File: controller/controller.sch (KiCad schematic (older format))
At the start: 30 parts, among them J1 Arduino_Nano_Header, P1 CONN_01X03, P2 CONN_01X03, P3 CONN_01X07, P4 CONN_01X02, SW1 DIPS_10, U1 MAX5024, U3 IL610, U4 MAX3040, U5 74LS165, U6 74LS165

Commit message: REV1 boards ordered
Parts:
- added P5: CONN_01X11, Pin_Headers:Pin_Header_Straight_1x11, symbol CONN_01X11
- added P6: CONN_01X08, Pin_Headers:Pin_Header_Straight_1x08, symbol CONN_01X08
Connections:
- net +5V: now also J1.30 (VIN); no longer J1.27 (5V)
- net DATA: now also P5.10 (P10)
- net DXM_OK: now also P5.8 (P8)
- net LATCH: now also P5.9 (P9)
- net at J1.8 (D5/T1), U4.1 (T1IN): now also P5.4 (P4)
- net at J1.7 (D4/T0), U4.7 (T2IN): now also P5.3 (P3)
- net at J1.10 (D7/AIN1): now also P5.6 (P6)
- net at J1.11 (D8/ICP): now also P5.7 (P7)
- net at J1.15 (D12/MISO): now also P5.11 (P11)
- net at J1.19 (A0): now also P6.8 (P8)
- net at J1.20 (A1): now also P6.7 (P7)
- net at J1.21 (A2): now also P6.6 (P6)
- net at J1.22 (A3): now also P6.5 (P5)
- net at J1.23 (A4): now also P6.4 (P4)
- net at J1.24 (A5): now also P6.3 (P3)
- net at J1.25 (A6): now also P6.2 (P2)
- net at C7.1, J1.26 (A7), RV1.2: now also P6.1 (P1)
- net RESET: now reaches J1.28 (RESET)
- net RESET: now also U1.4 (~RESET)
- net at J1.5 (D2/INT0): now also P5.1 (P1)
- net at J1.6 (D3/INT1): now also P5.2 (P2)
- net at J1.9 (D6/AIN0): now also P5.5 (P5)

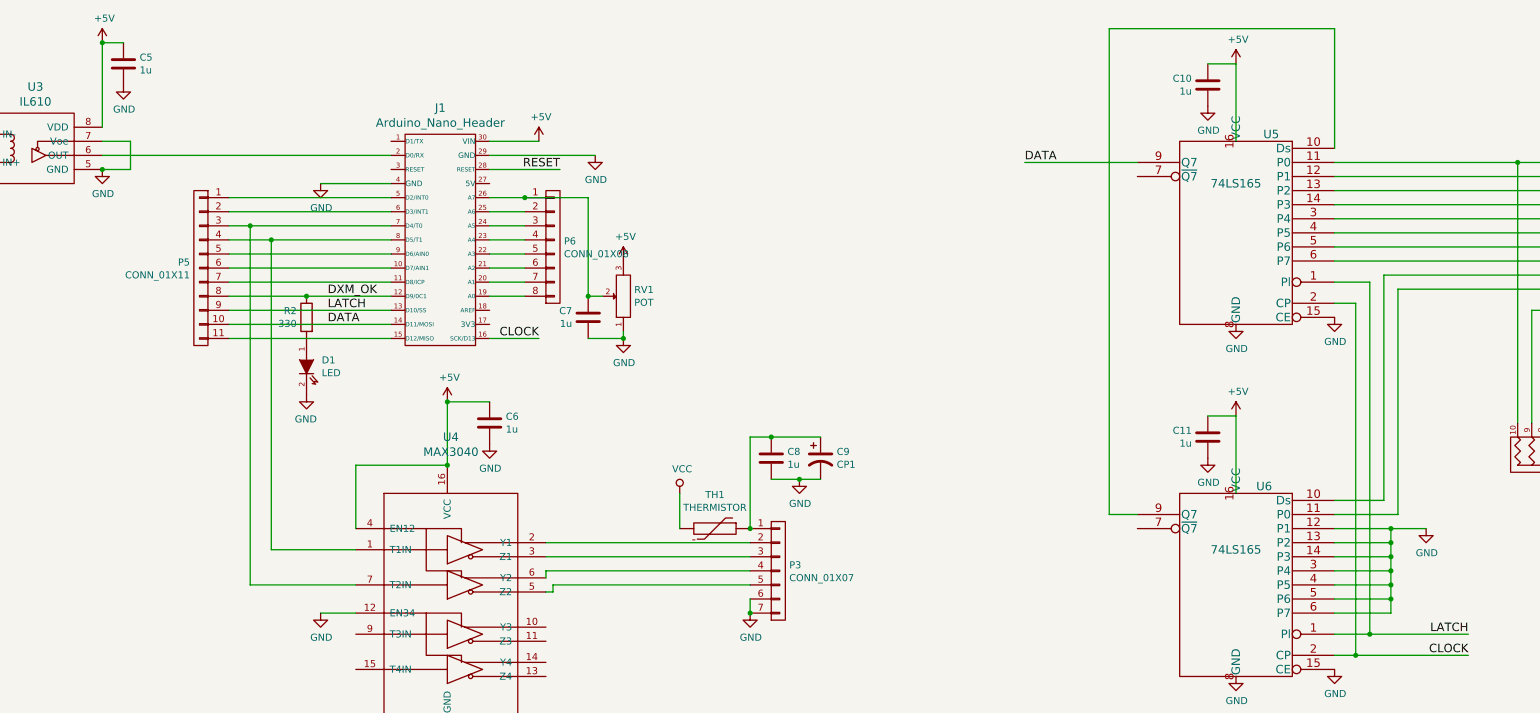
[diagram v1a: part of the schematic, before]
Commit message: Add fixes: control receiver enable line from Arduino so it does not interfere with programming; move data line to MISO pin so that we can read dip switch via SPI; fix routing for U6;
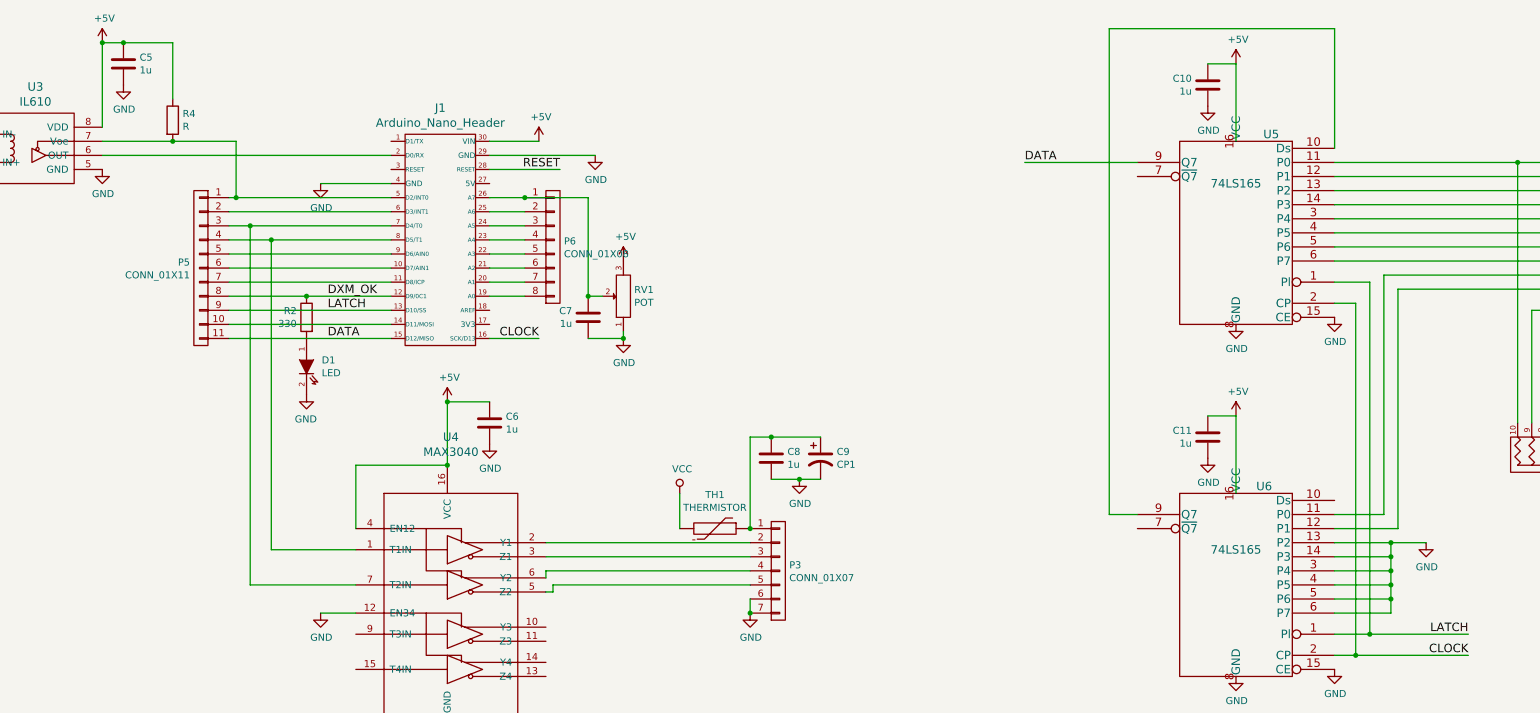
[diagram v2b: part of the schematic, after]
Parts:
- added R4: R, Resistors_SMD:R_0603_HandSoldering, symbol R
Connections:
- net +5V: now also R4.1
- net DATA: now also J1.15 (D12/MISO), P5.11 (P11); no longer J1.14 (D11/MOSI), P5.10 (P10)
- net GND: no longer U3.7 (Voe), U6.12 (P1)
- net at J1.5 (D2/INT0), P5.1 (P1): now also U3.7 (Voe), R4.2
- net at R1.1, SW1.11: now also U6.12 (P1); no longer U6.11 (P0)
- net at RP1.2 (P2), SW1.12: now also U6.11 (P0); no longer U6.10 (Ds)
- new net: J1.14 (D11/MOSI), P5.10 (P10)
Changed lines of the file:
@@
 LIBS:contrib
 LIBS:valves
-LIBS:max3096
 LIBS:w_connectors
 LIBS:dips-s
+LIBS:max3096
 LIBS:controller-cache
 EELAYER 25 0
@@
 L GND #PWR32
 U 1 1 571643DD
-P 12500 4450
-F 0 "#PWR32" H 12500 4200 50  0001 C CNN
-F 1 "GND" H 12505 4277 50  0000 C CNN
-F 2 "" H 12500 4450 60  0000 C CNN
-F 3 "" H 12500 4450 60  0000 C CNN
-	1    12500 4450
+P 12500 4550
+F 0 "#PWR32" H 12500 4300 50  0001 C CNN
+F 1 "GND" H 12505 4377 50  0000 C CNN
+F 2 "" H 12500 4550 60  0000 C CNN
+F 3 "" H 12500 4550 60  0000 C CNN
+	1    12500 4550
 	1    0    0    -1
 $EndComp
@@
 	1    0    0    -1
 $EndComp
-Text Label 4700 3000 0    60   ~ 0
+Text Label 4700 3100 0    60   ~ 0
 DATA
 Text Label 6200 3100 2    60   ~ 0
@@
 Connection ~ 7100 8150
 Wire Wire Line
-	3250 1000 3100 1000
+	3100 1000 3600 1000
 Wire Wire Line
 	3100 1000 3100 1600
 Connection ~ 3100 1000
-Wire Wire Line
-	3100 1700 3300 1700
-Wire Wire Line
-	3300 1700 3300 1900
-Wire Wire Line
-	3300 1900 3100 1900
-Connection ~ 3100 1900
 Wire Wire Line
 	5150 1800 3100 1800
@@
 	11850 5200 12800 5200
 Wire Wire Line
-	12200 2650 12200 4250
-Wire Wire Line
-	12200 4250 11850 4250
-Wire Wire Line
-	12300 2750 12300 4350
-Wire Wire Line
-	12300 4350 11850 4350
-Wire Wire Line
-	11850 4450 12500 4450
+	12300 2750 12300 4450
 Wire Wire Line
 	12250 5050 11850 5050
 Wire Wire Line
-	12250 4450 12250 5050
-Connection ~ 12250 4450
-Wire Wire Line
-	11850 4950 12250 4950
+	12250 4950 11850 4950
 Connection ~ 12250 4950
 Wire Wire Line
-	11850 4850 12250 4850
+	12250 4850 11850 4850
 Connection ~ 12250 4850
 Wire Wire Line
-	11850 4750 12250 4750
+	12250 4750 11850 4750
 Connection ~ 12250 4750
 Wire Wire Line
@@
 Connection ~ 12250 4650
 Wire Wire Line
-	11850 4550 12250 4550
+	11850 4550 12500 4550
 Connection ~ 12250 4550
 Connection ~ 12100 5200
@@
 $EndComp
 Wire Wire Line
-	5150 2100 4000 2100
+	4000 2100 5150 2100
 Wire Wire Line
 	5150 2200 4000 2200
@@
 Wire Wire Line
 	6100 2800 5850 2800
+$Comp
+L R R4
+U 1 1 571FBE18
+P 3600 1550
+F 0 "R4" H 3670 1596 50  0000 L CNN
+F 1 "R" H 3670 1505 50  0000 L CNN
+F 2 "Resistors_SMD:R_0603_HandSoldering" V 3530 1550 30  0001 C CNN
+F 3 "" H 3600 1550 30  0000 C CNN
+	1    3600 1550
+	1    0    0    -1
+$EndComp
+Wire Wire Line
+	3100 1700 4050 1700
+Wire Wire Line
+	3600 1000 3600 1400
+Connection ~ 3250 1000
+Wire Wire Line
+	4050 1700 4050 2100
+Connection ~ 4050 2100
+Connection ~ 3600 1700
 Connection ~ 6100 2100
+Wire Wire Line
+	12250 4550 12250 5050
+Wire Wire Line
+	12300 4450 11850 4450
+Wire Wire Line
+	12200 2650 12200 4350
+Wire Wire Line
+	12200 4350 11850 4350
 $EndSCHEMATC

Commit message: Add fixes to PCB
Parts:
- removed P5: CONN_01X11, Pin_Headers:Pin_Header_Straight_1x11, symbol CONN_01X11
- added P5: CONN_01X10, symbol CONN_01X10
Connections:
- net DATA: now also P5.10 (P10)
- net DXM_OK: now also P5.7 (P7)
- net LATCH: now also P5.8 (P8)
- net at J1.8 (D5/T1), U4.1 (T1IN): now also P5.3 (P3)
- net at J1.7 (D4/T0), U4.7 (T2IN): now also P5.2 (P2)
- net at J1.10 (D7/AIN1): now also P5.5 (P5)
- net at J1.11 (D8/ICP): now also P5.6 (P6)
- net at J1.14 (D11/MOSI): now also P5.9 (P9)
- net at J1.6 (D3/INT1): now also P5.1 (P1)
- net at J1.9 (D6/AIN0): now also P5.4 (P4)
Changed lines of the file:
@@
 taupyti elektrą:\n* tiny441 vietoj arduino?
 Wire Wire Line
-	6300 8150 7100 8150
-Wire Wire Line
-	4150 8450 4650 8450
+	6300 8150 6450 8150
+Wire Wire Line
+	6450 8150 6800 8150
+Wire Wire Line
+	6800 8150 7100 8150
+Wire Wire Line
+	4150 8450 4500 8450
+Wire Wire Line
+	4500 8450 4650 8450
 Connection ~ 7100 8450
 Connection ~ 4500 8450
 Wire Wire Line
-	3400 8150 5000 8150
+	3400 8150 4150 8150
+Wire Wire Line
+	4150 8150 4500 8150
+Wire Wire Line
+	4500 8150 4850 8150
+Wire Wire Line
+	4850 8150 5000 8150
 Connection ~ 4150 8150
 Connection ~ 7100 8150
 Wire Wire Line
-	3100 1000 3600 1000
+	3100 1000 3250 1000
+Wire Wire Line
+	3250 1000 3600 1000
 Wire Wire Line
 	3100 1000 3100 1600
@@
 Connection ~ 5550 3550
 Wire Wire Line
-	4000 2400 5150 2400
+	4000 2400 4300 2400
+Wire Wire Line
+	4300 2400 5150 2400
 Wire Wire Line
 	4300 2400 4300 4600
@@
 	4150 4850 4150 2300
 Wire Wire Line
-	4000 2300 5150 2300
-Wire Wire Line
-	1350 1850 2150 1850
-Wire Wire Line
-	1350 1750 1850 1750
+	4000 2300 4150 2300
+Wire Wire Line
+	4150 2300 5150 2300
+Wire Wire Line
+	1350 1850 1650 1850
+Wire Wire Line
+	1650 1850 2150 1850
+Wire Wire Line
+	1350 1750 1550 1750
+Wire Wire Line
+	1550 1750 1850 1750
 Wire Wire Line
 	1850 1750 1850 1650
@@
 Connection ~ 7700 5050
 Wire Wire Line
-	7700 3800 8200 3800
+	7700 3800 7850 3800
+Wire Wire Line
+	7850 3800 8200 3800
 Connection ~ 7850 3800
 Wire Wire Line
-	7850 4100 8200 4100
+	7850 4100 8050 4100
+Wire Wire Line
+	8050 4100 8200 4100
 Connection ~ 8050 4100
 Wire Wire Line
@@
 Connection ~ 7700 4450
 Wire Wire Line
-	12300 2750 15050 2750
-Wire Wire Line
-	12200 2650 15050 2650
-Wire Wire Line
-	11850 2550 15050 2550
-Wire Wire Line
-	11850 2450 15050 2450
-Wire Wire Line
-	11850 2350 15050 2350
-Wire Wire Line
-	11850 2250 15050 2250
-Wire Wire Line
-	11850 2150 15050 2150
-Wire Wire Line
-	11850 2050 15050 2050
-Wire Wire Line
-	11850 1950 15050 1950
-Wire Wire Line
-	11850 1850 15050 1850
+	12300 2750 14950 2750
+Wire Wire Line
+	14950 2750 15050 2750
+Wire Wire Line
+	12200 2650 14750 2650
+Wire Wire Line
+	14750 2650 15050 2650
+Wire Wire Line
+	11850 2550 14550 2550
+Wire Wire Line
+	14550 2550 15050 2550
+Wire Wire Line
+	11850 2450 14350 2450
+Wire Wire Line
+	14350 2450 15050 2450
+Wire Wire Line
+	11850 2350 14150 2350
+Wire Wire Line
+	14150 2350 15050 2350
+Wire Wire Line
+	11850 2250 13950 2250
+Wire Wire Line
+	13950 2250 15050 2250
+Wire Wire Line
+	11850 2150 13750 2150
+Wire Wire Line
+	13750 2150 15050 2150
+Wire Wire Line
+	11850 2050 13550 2050
+Wire Wire Line
+	13550 2050 15050 2050
+Wire Wire Line
+	11850 1950 13350 1950
+Wire Wire Line
+	13350 1950 15050 1950
+Wire Wire Line
+	11850 1850 13150 1850
+Wire Wire Line
+	13150 1850 15050 1850
 Wire Wire Line
 	14950 2750 14950 3750
@@
 Connection ~ 13150 1850
 Wire Wire Line
-	15450 1650 15450 2750
+	15450 1650 15450 1850
+Wire Wire Line
+	15450 1850 15450 1950
+Wire Wire Line
+	15450 1950 15450 2050
+Wire Wire Line
+	15450 2050 15450 2150
+Wire Wire Line
+	15450 2150 15450 2250
+Wire Wire Line
+	15450 2250 15450 2350
+Wire Wire Line
+	15450 2350 15450 2450
+Wire Wire Line
+	15450 2450 15450 2550
+Wire Wire Line
+	15450 2550 15450 2650
+Wire Wire Line
+	15450 2650 15450 2750
 Connection ~ 15450 2650
 Connection ~ 15450 2550
@@
 	12100 2700 12100 5200
 Wire Wire Line
-	11850 5200 12800 5200
+	11850 5200 12100 5200
+Wire Wire Line
+	12100 5200 12800 5200
 Wire Wire Line
 	12300 2750 12300 4450
@@
 Connection ~ 12250 4650
 Wire Wire Line
-	11850 4550 12500 4550
+	11850 4550 12250 4550
+Wire Wire Line
+	12250 4550 12500 4550
 Connection ~ 12250 4550
 Connection ~ 12100 5200
 Wire Wire Line
-	11850 5350 12800 5350
+	11850 5350 12000 5350
+Wire Wire Line
+	12000 5350 12800 5350
 Wire Wire Line
 	10450 1850 9650 1850
@@
 	14050 3700 14450 3700
 Wire Wire Line
-	14450 3700 14450 4100
+	14450 3700 14450 4050
+Wire Wire Line
+	14450 4050 14450 4100
 Wire Wire Line
 	14950 4050 14450 4050
@@
 Connection ~ 6800 8150
 Wire Wire Line
-	6650 8450 7100 8450
+	6650 8450 6800 8450
+Wire Wire Line
+	6800 8450 7100 8450
 Wire Wire Line
 	5000 8250 4850 8250
@@
 Connection ~ 6450 8150
 Wire Wire Line
-	5850 2100 6550 2100
+	5850 2100 6100 2100
+Wire Wire Line
+	6100 2100 6550 2100
 Wire Wire Line
 	6550 2100 6550 2800
@@
 	7550 8100 7650 8100
 Wire Wire Line
-	4000 2800 5150 2800
+	4000 2800 4550 2800
+Wire Wire Line
+	4550 2800 5150 2800
 Wire Wire Line
 	5000 8450 4750 8450
@@
 Text Label 6350 1900 2    60   ~ 0
 RESET
-$Comp
-L CONN_01X11 P5
-U 1 1 5719060B
-P 3800 2600
-F 0 "P5" H 3878 2641 50  0000 L CNN
-F 1 "CONN_01X11" H 3878 2550 50  0000 L CNN
-F 2 "Pin_Headers:Pin_Header_Straight_1x11" H 3878 2504 60  0001 L CNN
-F 3 "" H 3800 2600 60  0000 C CNN
-F 4 "?" H 3800 2600 60  0001 C CNN "PartNo"
-F 5 "?" H 3800 2600 60  0001 C CNN "Manufacturer"
-F 6 "?" H 3800 2600 60  0001 C CNN "Distributor"
-	1    3800 2600
-	-1   0    0    -1
-$EndComp
-Wire Wire Line
-	4000 2100 5150 2100
+Wire Wire Line
+	4100 2100 5150 2100
 Wire Wire Line
 	5150 2200 4000 2200
@@
 $EndComp
 Wire Wire Line
-	3100 1700 4050 1700
+	3100 1700 3600 1700
+Wire Wire Line
+	3600 1700 4100 1700
 Wire Wire Line
 	3600 1000 3600 1400
 Connection ~ 3250 1000
 Wire Wire Line
-	4050 1700 4050 2100
-Connection ~ 4050 2100
+	4100 1700 4100 2100
 Connection ~ 3600 1700
 Connection ~ 6100 2100
 Wire Wire Line
-	12250 4550 12250 5050
+	12250 4550 12250 4650
+Wire Wire Line
+	12250 4650 12250 4750
+Wire Wire Line
+	12250 4750 12250 4850
+Wire Wire Line
+	12250 4850 12250 4950
+Wire Wire Line
+	12250 4950 12250 5050
 Wire Wire Line
 	12300 4450 11850 4450
@@
 Wire Wire Line
 	12200 4350 11850 4350
+$Comp
+L CONN_01X10 P5
+U 1 1 57207EFA
+P 3800 2650
+F 0 "P5" H 3878 2691 50  0000 L CNN
+F 1 "CONN_01X10" H 3878 2600 50  0000 L CNN
+F 2 "" H 3800 2650 60  0000 C CNN
+F 3 "" H 3800 2650 60  0000 C CNN
+F 4 "?" H 3800 2650 60  0001 C CNN "PartNo"
+F 5 "?" H 3800 2650 60  0001 C CNN "Manufacturer"
+F 6 "?" H 3800 2650 60  0001 C CNN "Distributor"
+	1    3800 2650
+	-1   0    0    -1
+$EndComp
 $EndSCHEMATC

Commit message: Forgotten commit at the end of project
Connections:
- net DXM_OK: now also J1.11 (D8/ICP), P5.6 (P6); no longer J1.12 (D9/0C1), P5.7 (P7)
- net at J1.8 (D5/T1), P5.3 (P3): no longer U4.1 (T1IN)
- net DIR: now reaches J1.7 (D4/T0), P5.2 (P2), U4.7 (T2IN)
- new net STEP: J1.12 (D9/0C1), P5.7 (P7), U4.1 (T1IN)
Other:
- moved on the sheet: D1, R2
